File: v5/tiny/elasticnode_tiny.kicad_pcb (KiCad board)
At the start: 4 copper layers, 34 x 34 mm, 125 parts, among them J1 P5KS_40PINSOCKET, J2 JUMPER3, J3 53261-0271, J4 USB4105-GF-A, J6 JUMPER3, J7 505278-2033, Q1 FDN302P, U1 LTC3569EUDPBF, U2 MCP73833T-AMI/MF, U3 ICE40UP50K, U4 PAC1934, U6 W25Q16JVUXIQ, U7 RP2040, U8 W25Q16JVUXIQ, X1 12MHz, X2 DSC6001H

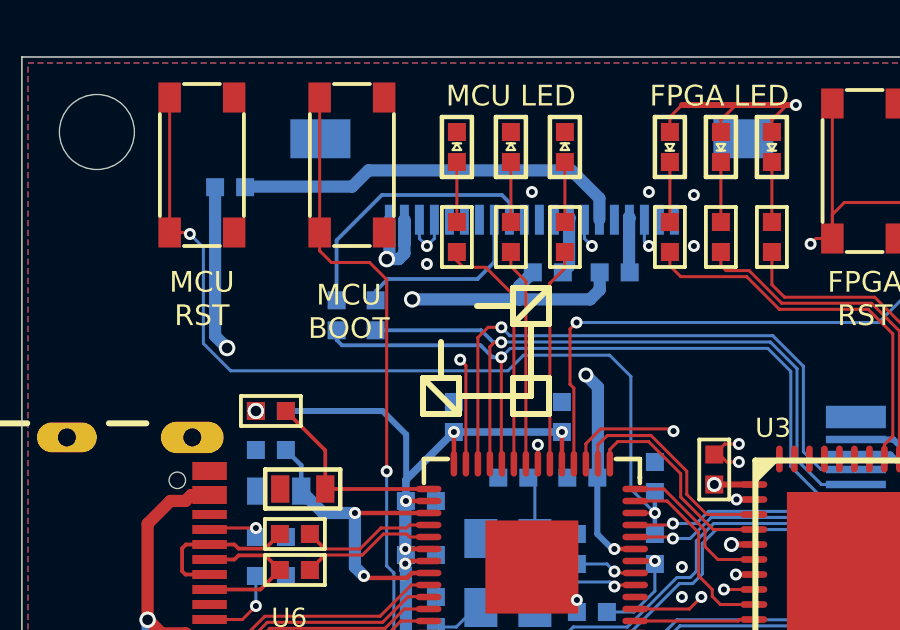
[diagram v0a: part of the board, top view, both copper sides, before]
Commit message: Add design of ENV6 mini
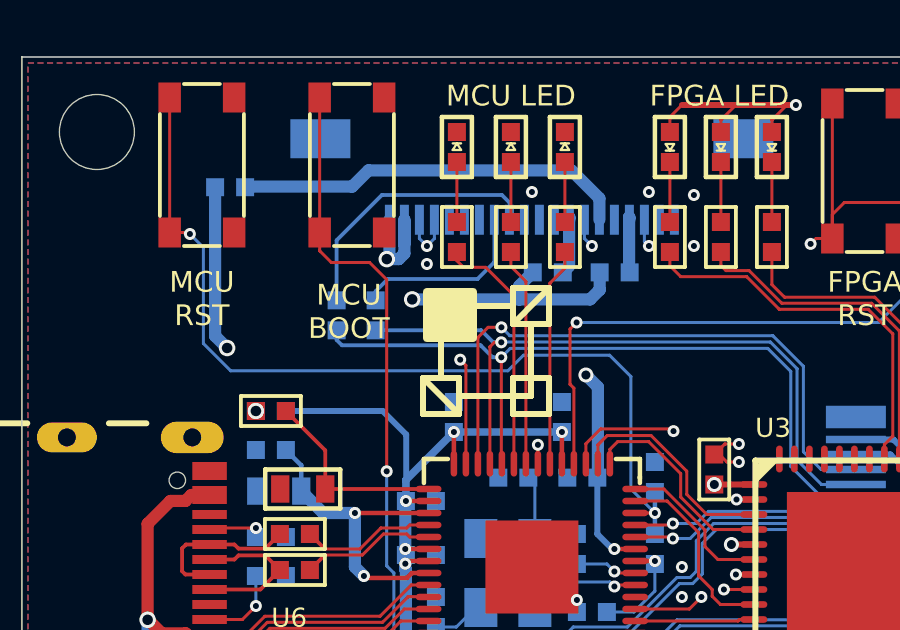
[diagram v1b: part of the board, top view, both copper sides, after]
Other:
- board text removed: "100R"
- board text removed: "499"
